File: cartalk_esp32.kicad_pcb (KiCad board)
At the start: 2 copper layers, 22.9 x 48.8 mm, 22 parts, among them IC1 CP2104, J1 10118192-0002LF, Q1 mmbt2222, Q2 mmbt2222, SW2 KMR2, U1 HUB75 Connector Female, U2 AP2112-3.3, X2 ESP32_WROOM32_SKINNY

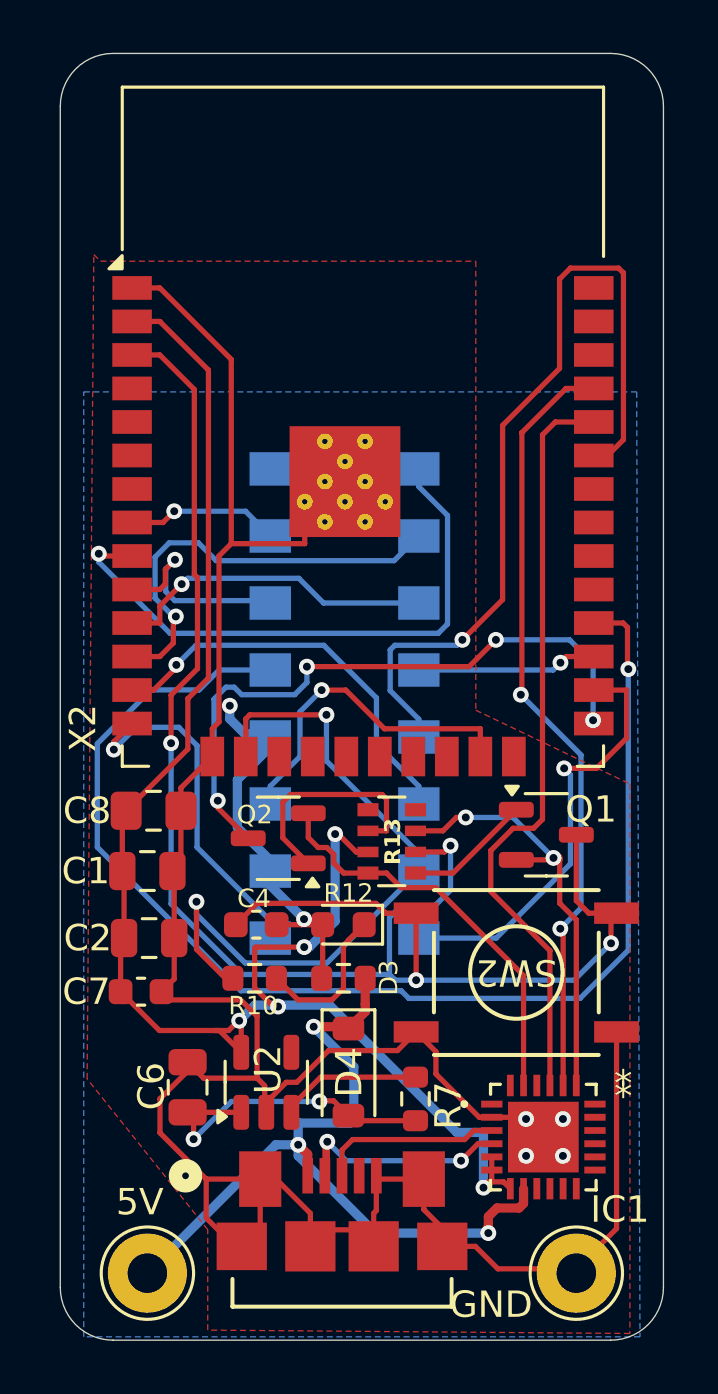
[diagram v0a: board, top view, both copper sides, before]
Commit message: Increase track width of 3.3V on F.Cu.
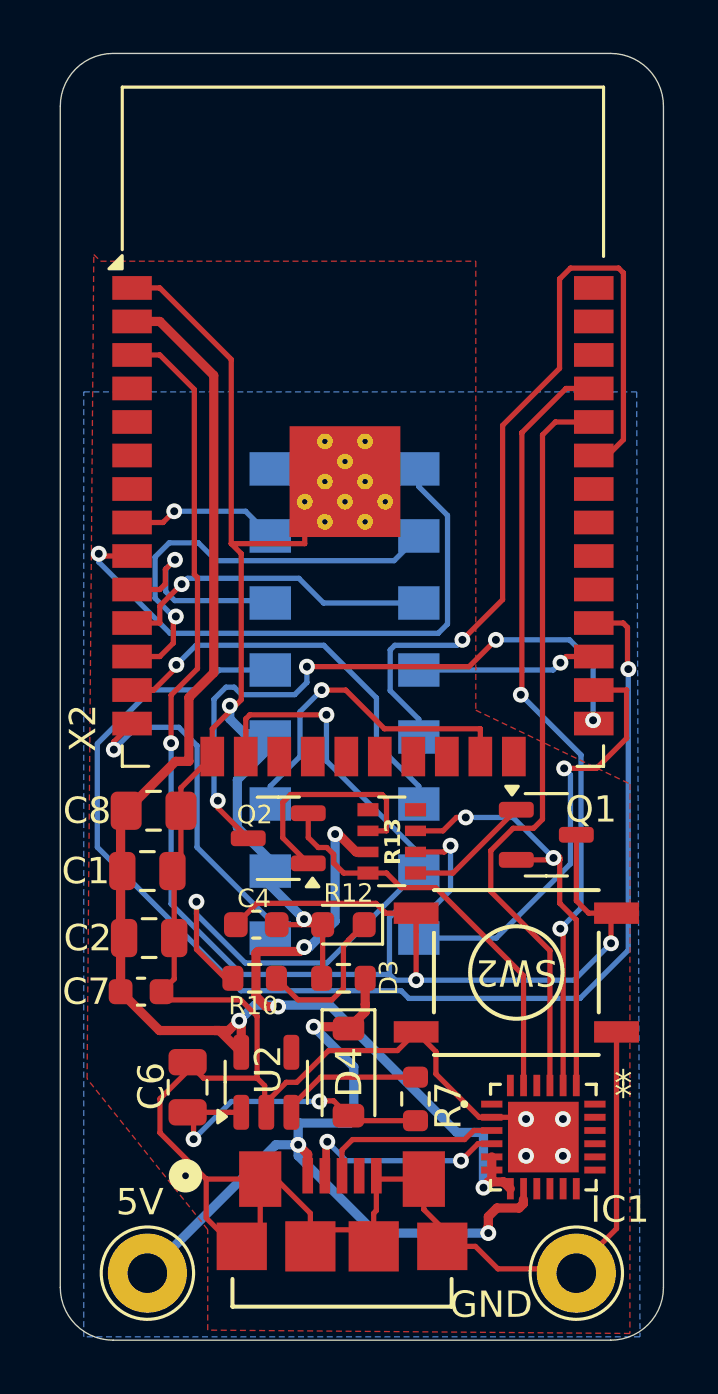
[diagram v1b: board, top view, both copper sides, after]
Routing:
- net 3.3V: track 63.3 -> 63.8 mm

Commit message: Increase track width of GND on F.Cu.
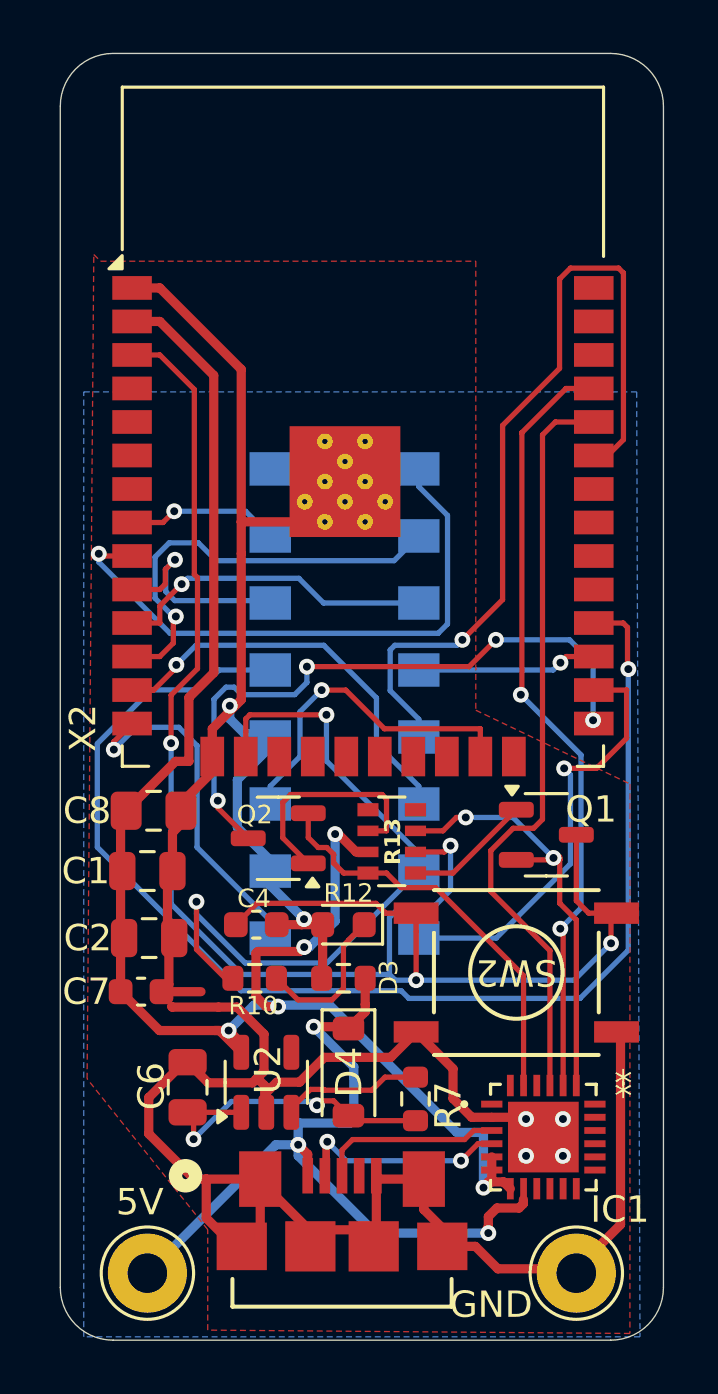
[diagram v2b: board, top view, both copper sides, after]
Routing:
- net GND: track 127.7 -> 130.0 mm

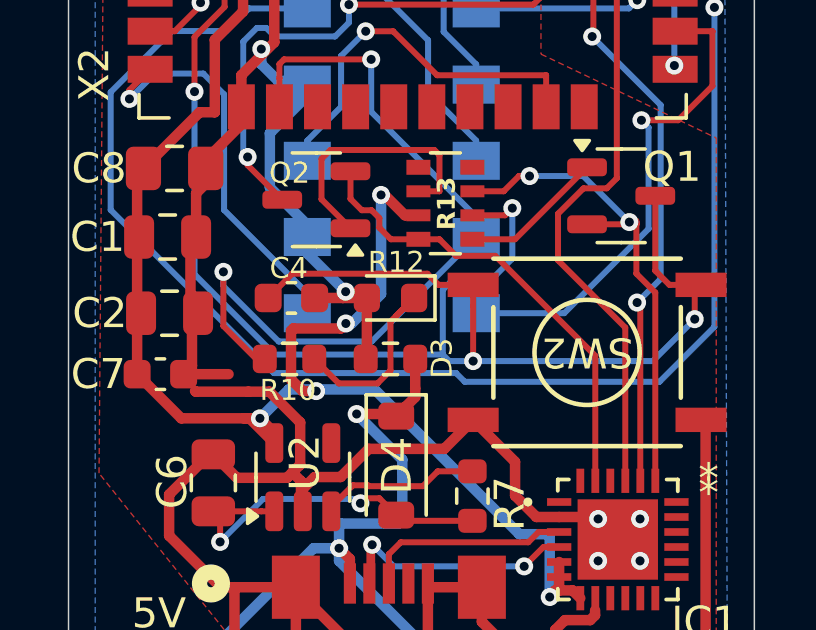
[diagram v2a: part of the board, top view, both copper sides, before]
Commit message: Swap silkscreen labels of D3 and R12 where they should be.
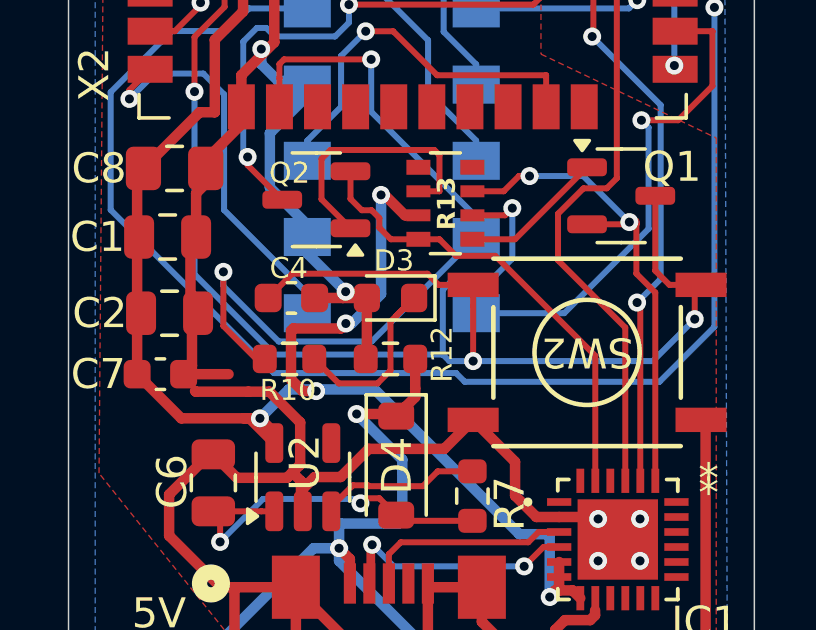
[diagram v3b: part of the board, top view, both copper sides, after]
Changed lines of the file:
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@@
 		(tags "resistor")
 		(property "Reference" "R12"
-			(at 0.191 -3.2258 0)
+			(at 1.715 -0.1524 -90)
 			(layer "F.SilkS")
 			(effects
@@
 			)
 		)
-		(sheetname "Root")
-		(sheetfile "cartalk_esp32.kicad_sch")
 		(attr smd)
 		(fp_line
@@
 		(tags "LED")
 		(property "Reference" "D3"
-			(at -1.715 -2.0066 -90)
-			(layer "F.SilkS")
-			(effects
+			(at -0.1148 1.2446 0)
+			(layer "F.SilkS")
+			(effects
